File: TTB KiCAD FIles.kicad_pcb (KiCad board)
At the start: 2 copper layers, 174.2 x 86.7 mm, 6 parts, among them J1 PJ-102A, J2 Conn_01x03_Pin, U1 Relay Module, U2 ESP32 Module, U3 Motor Driver, U4 Voltage Regulator

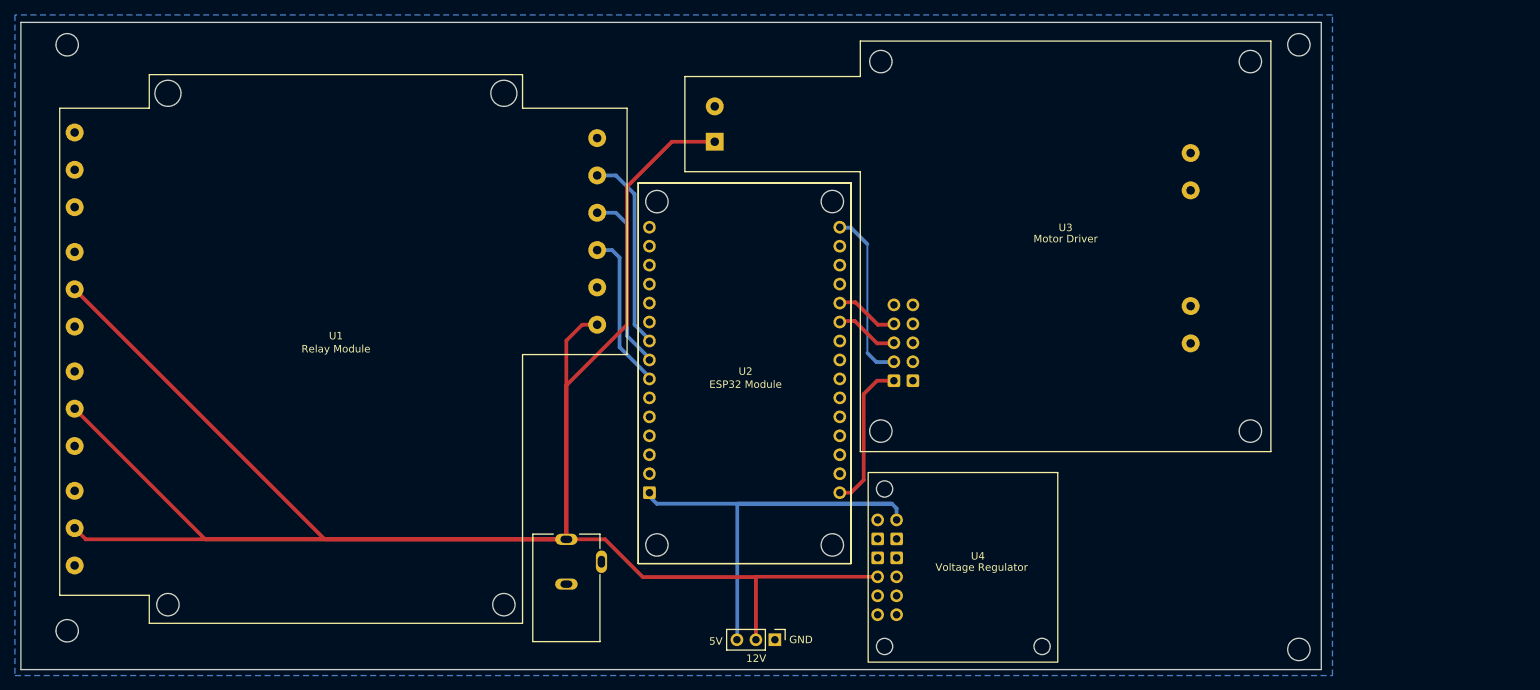
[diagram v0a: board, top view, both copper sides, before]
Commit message: Added Design Modifications
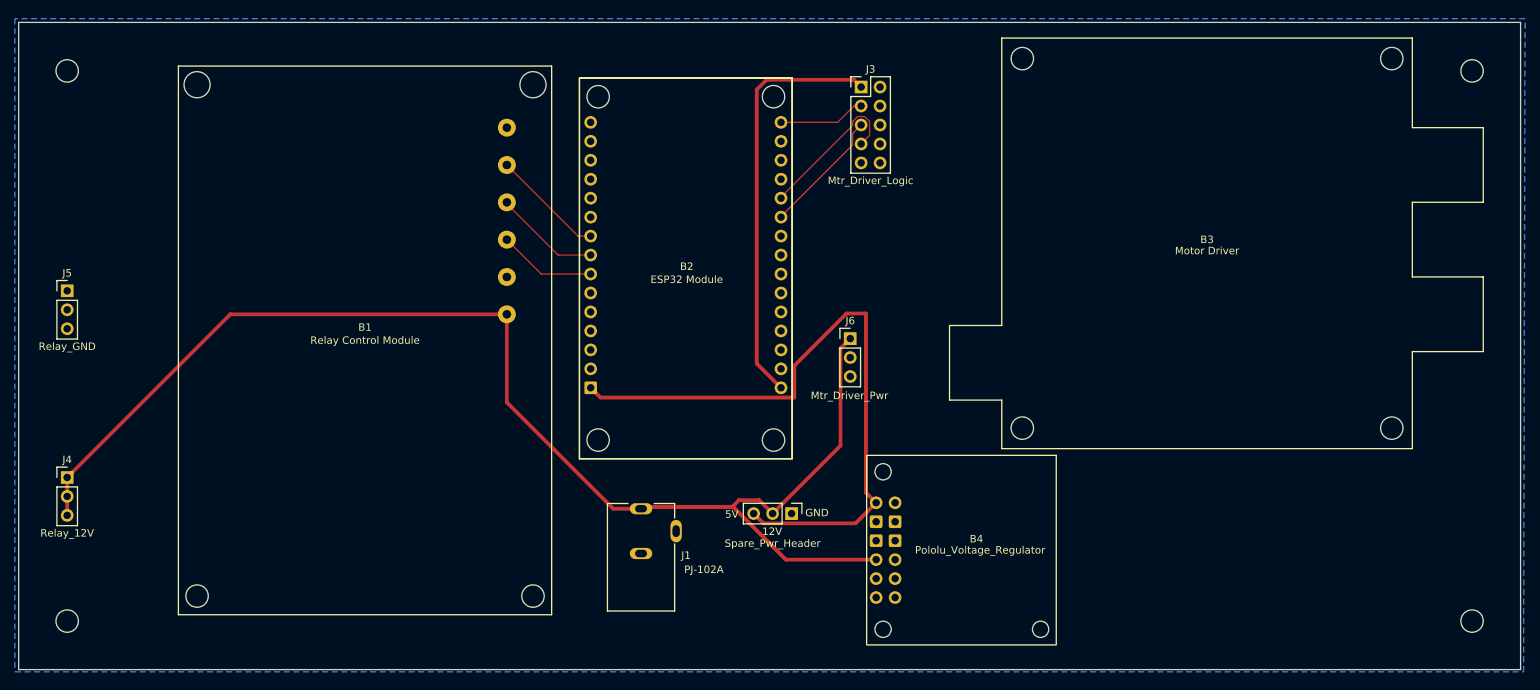
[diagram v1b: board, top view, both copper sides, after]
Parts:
- added J3: Mtr_Driver_Logic, Connector_PinHeader_2.54mm:PinHeader_2x05_P2.54mm_Vertical, F.Cu at (153.4, 53.7)
- added J4: Relay_12V, Connector_PinHeader_2.54mm:PinHeader_1x03_P2.54mm_Vertical, F.Cu at (47.0, 106.0)
- added J5: Relay_GND, Connector_PinHeader_2.54mm:PinHeader_1x03_P2.54mm_Vertical, F.Cu at (47.0, 81.0)
- added J6: Mtr_Driver_Pwr, Connector_PinHeader_2.54mm:PinHeader_1x03_P2.54mm_Vertical, F.Cu at (151.9, 87.4)
- B1: renamed from U1; value Relay Module -> Relay Control Module
- B3: renamed from U3; moved to F.Cu
- B4: renamed from U4; value Voltage Regulator -> Pololu_Voltage_Regulator
- J2: value Conn_01x03_Pin -> Spare_Pwr_Header
- moved B3 19.0 mm to (199.7, 74.6)
- moved J2 17.0 mm to (144.0, 110.8)
- moved B2 16.1 mm to (130.0, 78.2)
- moved J1 10.8 mm to (123.9, 113.2)
- moved B1 4.07 mm to (111.9, 50.9)
- moved B4 2.31 mm to (166.8, 115.7)
- renumbered U2 to B2
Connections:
- net Net-(U1-IN1) renamed /R1
- net Net-(U1-IN2) renamed /R2
- net Net-(U1-IN3) renamed /R3
- B2 pad 16: Net-(U2-3V3) -> /3.3V 
- B2 pad 25: Net-(U2-D19) -> /IN1
- B2 pad 26: Net-(U2-D21) -> /IN2
- B2 pad 30: Net-(U2-D23) -> /ENA
- B4 pad 7: +5V -> unconnected-(U4-VOUT-Pad7)
- B4 pad 8: unconnected-(U4-VOUT-Pad8) -> +5V
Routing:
- net +12V: track 368.1 -> 189.5 mm
- net /3.3V : track 0.00 -> 56.2 mm
- net Net-(U2-D23): track 22.8 -> 0.00 mm
- net /IN2: track 0.00 -> 20.5 mm
- net Net-(U2-3V3): track 19.7 -> 0.00 mm
- net /IN1: track 0.00 -> 16.8 mm
- net +5V: track 75.3 -> 88.6 mm
- net /ENA: track 0.00 -> 11.6 mm
- net /R3: track 26.4 -> 15.2 mm
- net /R2: track 23.9 -> 14.3 mm
- net Net-(U2-D21): track 7.99 -> 0.00 mm
- net Net-(U2-D19): track 7.99 -> 0.00 mm
- net /R1: track 21.1 -> 13.1 mm
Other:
- board size 174.2 x 86.7 mm -> 201.2 x 86.7 mm

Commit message: Clean up track wiring & add silkscreen clarification
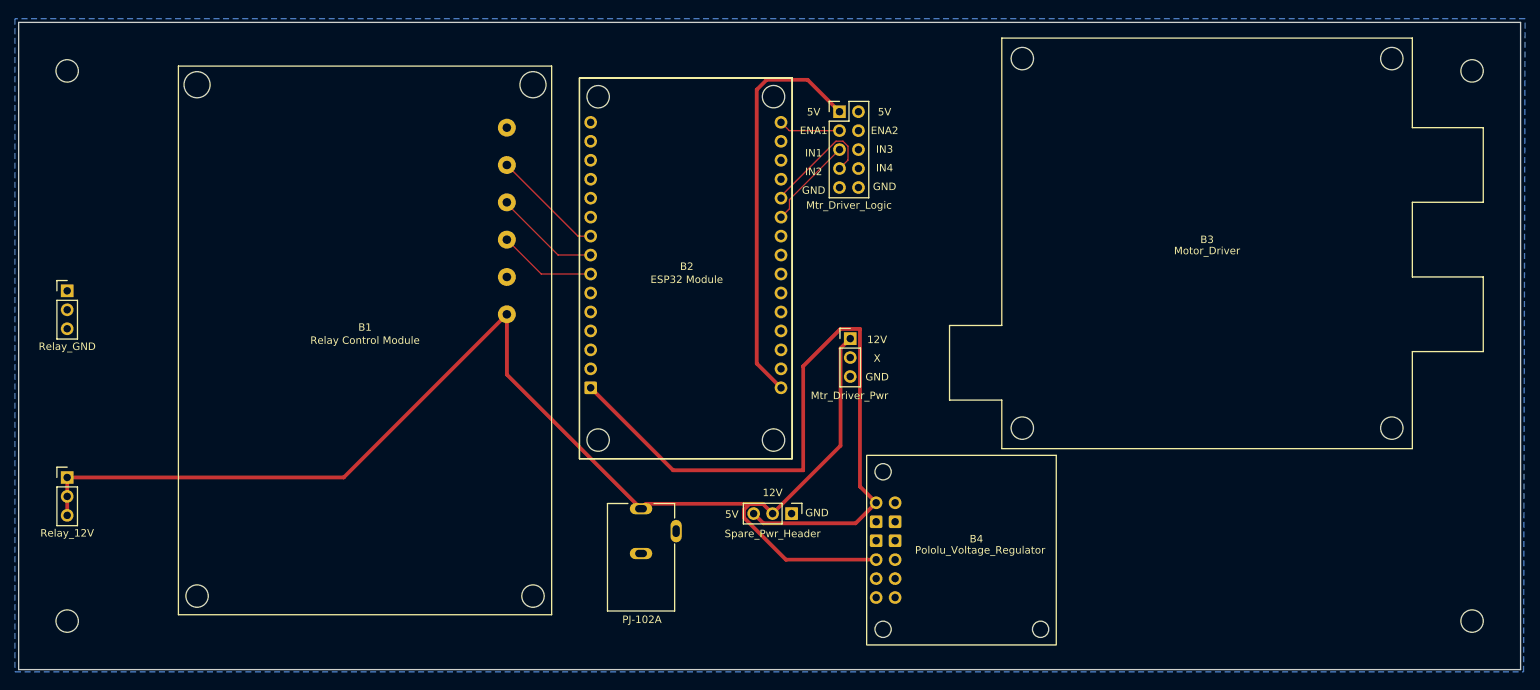
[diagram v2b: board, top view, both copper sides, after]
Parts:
- B3: value Motor Driver -> Motor_Driver
- moved J3 4.39 mm to (150.5, 57.0)
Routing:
- net +12V: track 189.5 -> 176.7 mm
- net +5V: track 88.6 -> 99.0 mm
- net /IN1: track 16.8 -> 12.3 mm
- net /IN2: track 20.5 -> 16.0 mm
- net /ENA: track 11.6 -> 8.29 mm
- net /3.3V : track 56.2 -> 54.7 mm
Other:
- board text added: "ENA1"
- board text added: "ENA2"
- board text added: "IN1"
- board text added: "IN2"
- board text added: "IN3"
- board text added: "IN4"
- board text added: "X"
